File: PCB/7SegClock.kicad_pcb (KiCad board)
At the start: 2 copper layers, 177.8 x 76.2 mm, 41 parts, among them CON1 USB-MINI-B, Q1 NPN, U1 P8X32A, U2 24LC256, U3 FT232RL, U4 DS3231, U5 TPS62172DSGT, U6 LCMX02-640UHC-4TG144C, X1 5mhz CRYSTAL

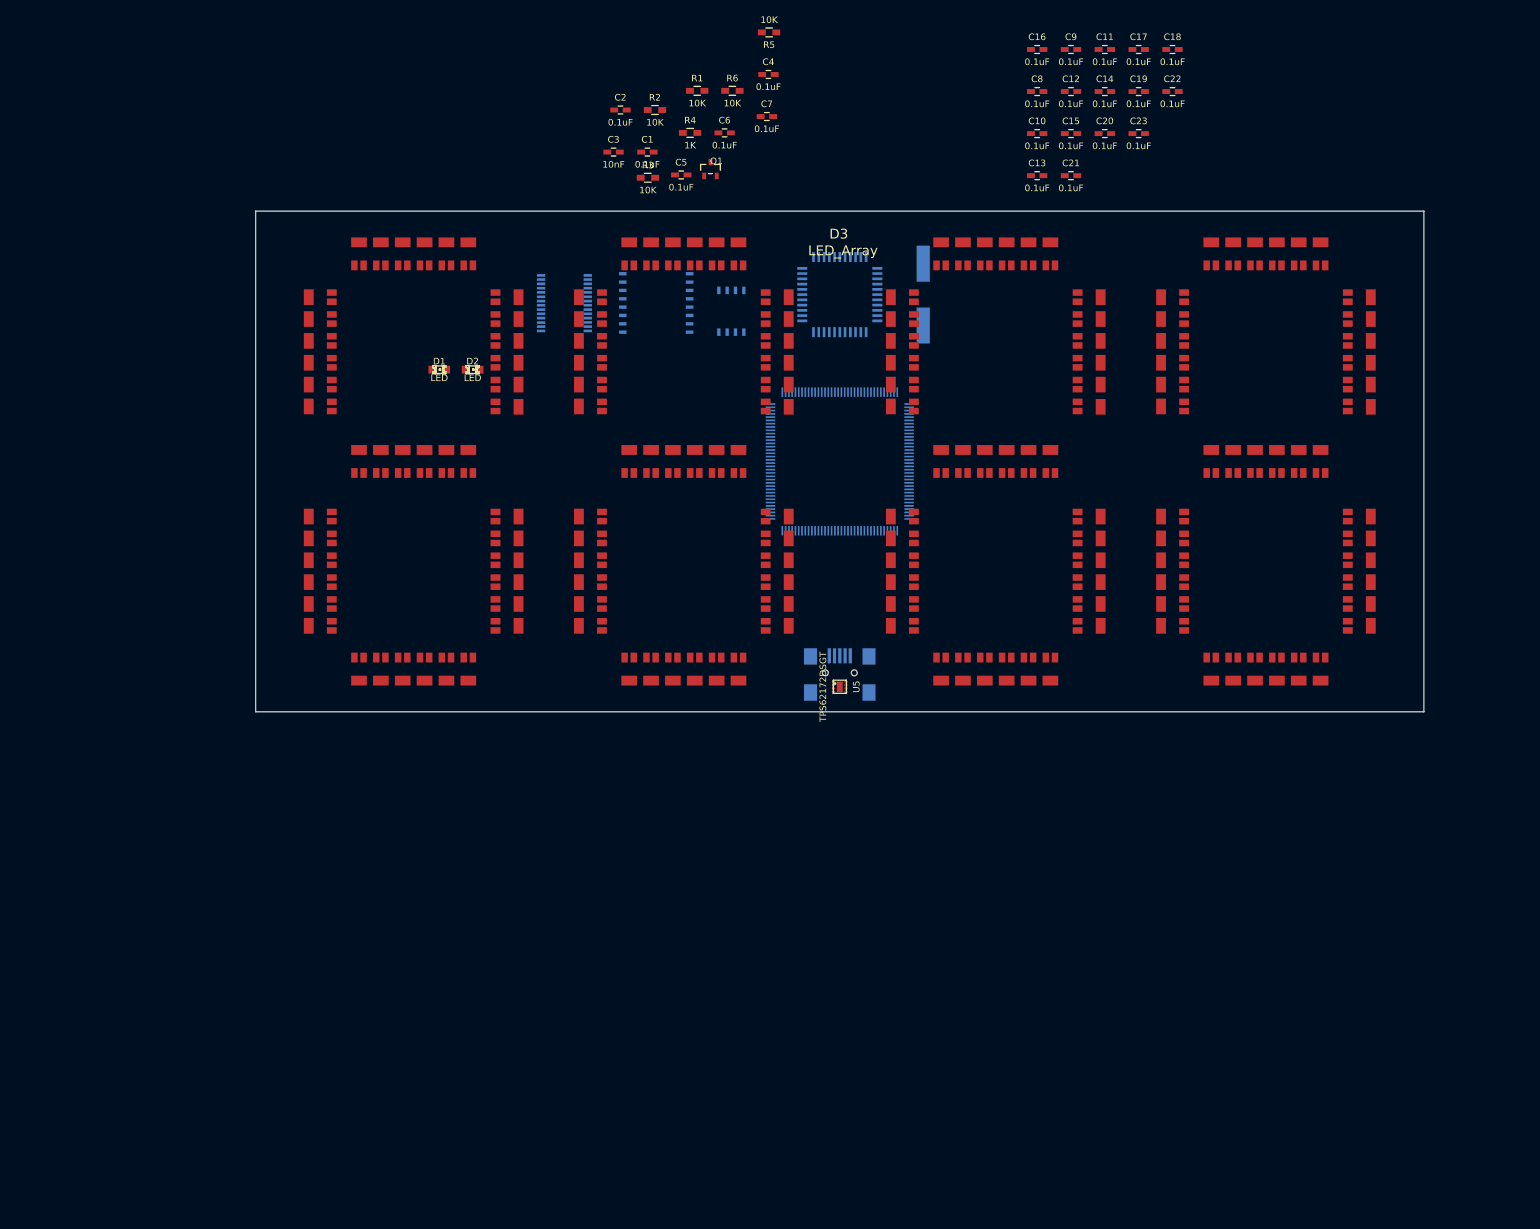
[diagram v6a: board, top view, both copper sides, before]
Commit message: Added additional mosfets.
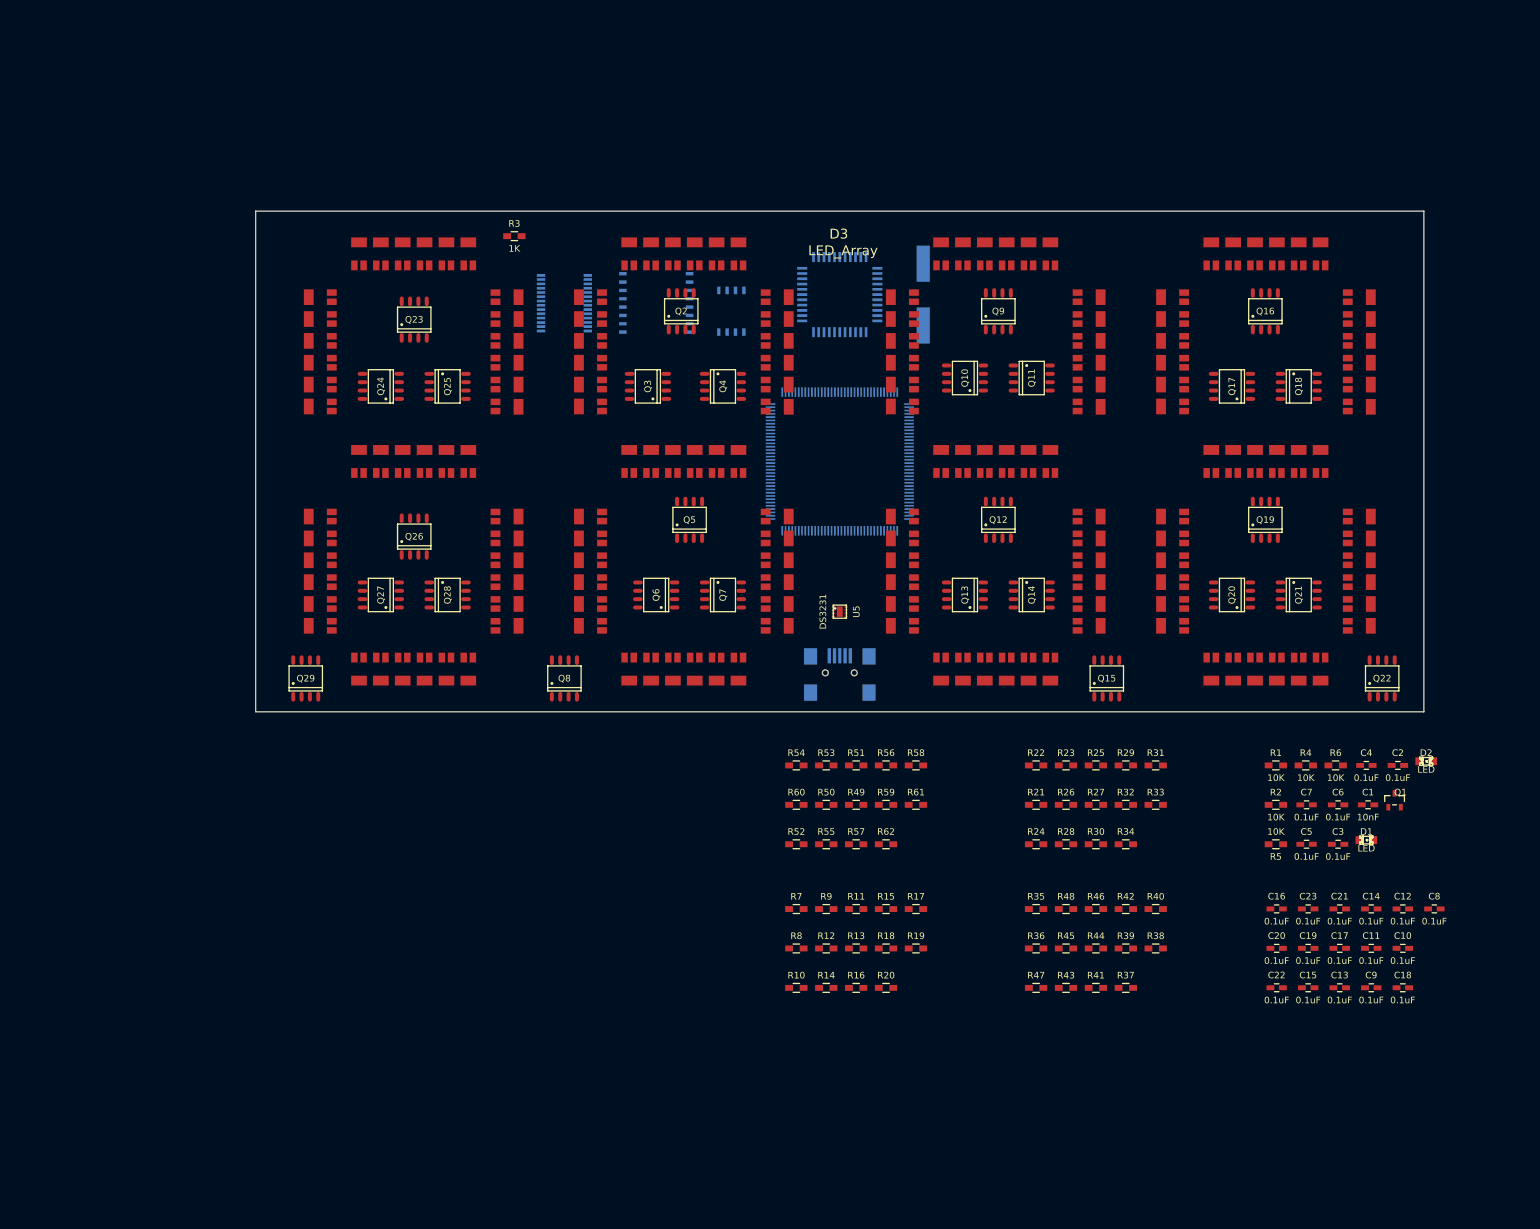
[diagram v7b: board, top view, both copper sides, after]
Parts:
- added Q10: DMN2041LSD-13, SO-8, F.Cu at (167.6, 73.7)
- added Q11: DMN2041LSD-13, SO-8, F.Cu at (177.8, 73.7)
- added Q12: DMN2041LSD-13, SO-8, F.Cu at (172.7, 95.2)
- added Q13: DMN2041LSD-13, SO-8, F.Cu at (167.6, 106.7)
- added Q14: DMN2041LSD-13, SO-8, F.Cu at (177.8, 106.7)
- added Q15: DMN2041LSD-13, SO-8, F.Cu at (189.2, 119.4)
- added Q16: DMN2041LSD-13, SO-8, F.Cu at (213.4, 63.5)
- added Q17: DMN2041LSD-13, SO-8, F.Cu at (208.3, 74.9)
- added Q18: DMN2041LSD-13, SO-8, F.Cu at (218.4, 74.9)
- added Q19: DMN2041LSD-13, SO-8, F.Cu at (213.4, 95.2)
- added Q2: DMN2041LSD-13, SO-8, F.Cu at (124.5, 63.5)
- added Q20: DMN2041LSD-13, SO-8, F.Cu at (208.3, 106.7)
- added Q21: DMN2041LSD-13, SO-8, F.Cu at (218.4, 106.7)
- added Q22: DMN2041LSD-13, SO-8, F.Cu at (231.1, 119.4)
- added Q23: DMN2041LSD-13, SO-8, F.Cu at (83.8, 64.8)
- added Q24: DMN2041LSD-13, SO-8, F.Cu at (78.7, 74.9)
- added Q25: DMN2041LSD-13, SO-8, F.Cu at (88.9, 74.9)
- added Q26: DMN2041LSD-13, SO-8, F.Cu at (83.8, 97.8)
- added Q27: DMN2041LSD-13, SO-8, F.Cu at (78.7, 106.7)
- added Q28: DMN2041LSD-13, SO-8, F.Cu at (88.9, 106.7)
- added Q29: DMN2041LSD-13, SO-8, F.Cu at (67.3, 119.4)
- added Q3: DMN2041LSD-13, SO-8, F.Cu at (119.4, 74.9)
- added Q4: DMN2041LSD-13, SO-8, F.Cu at (130.8, 74.9)
- added Q5: DMN2041LSD-13, SO-8, F.Cu at (125.7, 95.2)
- added Q6: DMN2041LSD-13, SO-8, F.Cu at (120.7, 106.7)
- added Q7: DMN2041LSD-13, SO-8, F.Cu at (130.8, 106.7)
- added Q8: DMN2041LSD-13, SO-8, F.Cu at (106.7, 119.4)
- added Q9: DMN2041LSD-13, SO-8, F.Cu at (172.7, 63.5)
- added R10: 10K, Resistors_SMD:R_0603_HandSoldering, F.Cu at (142.0, 166.5)
- added R11: 10K, Resistors_SMD:R_0603_HandSoldering, F.Cu at (151.1, 154.5)
- added R12: 10K, Resistors_SMD:R_0603_HandSoldering, F.Cu at (146.5, 160.5)
- added R13: 10K, Resistors_SMD:R_0603_HandSoldering, F.Cu at (151.1, 160.5)
- added R14: 10K, Resistors_SMD:R_0603_HandSoldering, F.Cu at (146.5, 166.5)
- added R15: 10K, Resistors_SMD:R_0603_HandSoldering, F.Cu at (155.6, 154.5)
- added R16: 10K, Resistors_SMD:R_0603_HandSoldering, F.Cu at (151.1, 166.5)
- added R17: 10K, Resistors_SMD:R_0603_HandSoldering, F.Cu at (160.2, 154.5)
- added R18: 10K, Resistors_SMD:R_0603_HandSoldering, F.Cu at (155.6, 160.5)
- added R19: 10K, Resistors_SMD:R_0603_HandSoldering, F.Cu at (160.2, 160.5)
- added R20: 10K, Resistors_SMD:R_0603_HandSoldering, F.Cu at (155.6, 166.5)
- added R21: 10K, Resistors_SMD:R_0603_HandSoldering, F.Cu at (178.5, 138.6)
- added R22: 10K, Resistors_SMD:R_0603_HandSoldering, F.Cu at (178.5, 132.6)
- added R23: 10K, Resistors_SMD:R_0603_HandSoldering, F.Cu at (183.0, 132.6)
- added R24: 10K, Resistors_SMD:R_0603_HandSoldering, F.Cu at (178.5, 144.6)
- added R25: 10K, Resistors_SMD:R_0603_HandSoldering, F.Cu at (187.6, 132.6)
- added R26: 10K, Resistors_SMD:R_0603_HandSoldering, F.Cu at (183.0, 138.6)
- added R27: 10K, Resistors_SMD:R_0603_HandSoldering, F.Cu at (187.6, 138.6)
- added R28: 10K, Resistors_SMD:R_0603_HandSoldering, F.Cu at (183.0, 144.6)
- added R29: 10K, Resistors_SMD:R_0603_HandSoldering, F.Cu at (192.1, 132.6)
- added R30: 10K, Resistors_SMD:R_0603_HandSoldering, F.Cu at (187.6, 144.6)
- added R31: 10K, Resistors_SMD:R_0603_HandSoldering, F.Cu at (196.7, 132.6)
- added R32: 10K, Resistors_SMD:R_0603_HandSoldering, F.Cu at (192.1, 138.6)
- added R33: 10K, Resistors_SMD:R_0603_HandSoldering, F.Cu at (196.7, 138.6)
- added R34: 10K, Resistors_SMD:R_0603_HandSoldering, F.Cu at (192.1, 144.6)
- added R35: 10K, Resistors_SMD:R_0603_HandSoldering, F.Cu at (178.5, 154.5)
- added R36: 10K, Resistors_SMD:R_0603_HandSoldering, F.Cu at (178.5, 160.5)
- added R37: 10K, Resistors_SMD:R_0603_HandSoldering, F.Cu at (192.1, 166.5)
- added R38: 10K, Resistors_SMD:R_0603_HandSoldering, F.Cu at (196.7, 160.5)
- added R39: 10K, Resistors_SMD:R_0603_HandSoldering, F.Cu at (192.1, 160.5)
- added R40: 10K, Resistors_SMD:R_0603_HandSoldering, F.Cu at (196.7, 154.5)
- added R41: 10K, Resistors_SMD:R_0603_HandSoldering, F.Cu at (187.6, 166.5)
- added R42: 10K, Resistors_SMD:R_0603_HandSoldering, F.Cu at (192.1, 154.5)
- added R43: 10K, Resistors_SMD:R_0603_HandSoldering, F.Cu at (183.0, 166.5)
- added R44: 10K, Resistors_SMD:R_0603_HandSoldering, F.Cu at (187.6, 160.5)
- added R45: 10K, Resistors_SMD:R_0603_HandSoldering, F.Cu at (183.0, 160.5)
- added R46: 10K, Resistors_SMD:R_0603_HandSoldering, F.Cu at (187.6, 154.5)
- added R47: 10K, Resistors_SMD:R_0603_HandSoldering, F.Cu at (178.5, 166.5)
- added R48: 10K, Resistors_SMD:R_0603_HandSoldering, F.Cu at (183.0, 154.5)
- added R49: 10K, Resistors_SMD:R_0603_HandSoldering, F.Cu at (151.1, 138.6)
- added R50: 10K, Resistors_SMD:R_0603_HandSoldering, F.Cu at (146.5, 138.6)
- added R51: 10K, Resistors_SMD:R_0603_HandSoldering, F.Cu at (151.1, 132.6)
- added R52: 10K, Resistors_SMD:R_0603_HandSoldering, F.Cu at (142.0, 144.6)
- added R53: 10K, Resistors_SMD:R_0603_HandSoldering, F.Cu at (146.5, 132.6)
- added R54: 10K, Resistors_SMD:R_0603_HandSoldering, F.Cu at (142.0, 132.6)
- added R55: 10K, Resistors_SMD:R_0603_HandSoldering, F.Cu at (146.5, 144.6)
- added R56: 10K, Resistors_SMD:R_0603_HandSoldering, F.Cu at (155.6, 132.6)
- added R57: 10K, Resistors_SMD:R_0603_HandSoldering, F.Cu at (151.1, 144.6)
- added R58: 10K, Resistors_SMD:R_0603_HandSoldering, F.Cu at (160.2, 132.6)
- added R59: 10K, Resistors_SMD:R_0603_HandSoldering, F.Cu at (155.6, 138.6)
- added R60: 10K, Resistors_SMD:R_0603_HandSoldering, F.Cu at (142.0, 138.6)
- added R61: 10K, Resistors_SMD:R_0603_HandSoldering, F.Cu at (160.2, 138.6)
- added R62: 10K, Resistors_SMD:R_0603_HandSoldering, F.Cu at (155.6, 144.6)
- added R7: 10K, Resistors_SMD:R_0603_HandSoldering, F.Cu at (142.0, 154.5)
- added R8: 10K, Resistors_SMD:R_0603_HandSoldering, F.Cu at (142.0, 160.5)
- added R9: 10K, Resistors_SMD:R_0603_HandSoldering, F.Cu at (146.5, 154.5)
- C1: value 0.1uF -> 10nF
- C3: value 10nF -> 0.1uF
- R3: value 10K -> 1K
- R4: value 1K -> 10K
- U1: value P8X32A -> TPS62172DSGT
- U2: value 24LC256 -> P8X32A
- U4: value DS3231 -> 24LC256
- U5: value TPS62172DSGT -> DS3231
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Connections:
- C1 pad 1: GND -> Net-(C1-Pad1)
- C1 pad 2: +3V3 -> Net-(C1-Pad2)
- C3 pad 1: Net-(C3-Pad1) -> GND
- C3 pad 2: Net-(C3-Pad2) -> +3V3
- D3 pad 1: Net-(D3-Pad1) -> /Lattice MACHXO2/Digit_1/D1A1
- D3 pad 10: Net-(D3-Pad10) -> /Lattice MACHXO2/Digit_1/D1A4
- D3 pad 100: Net-(D3-Pad100) -> /Lattice MACHXO2/Digit_1/D1A4
- D3 pad 103: Net-(D3-Pad103) -> /Lattice MACHXO2/Digit_1/D1A5
- D3 pad 104: Net-(D3-Pad104) -> Net-(D3-Pad101)
- D3 pad 105: Net-(D3-Pad105) -> Net-(D3-Pad102)
- D3 pad 106: Net-(D3-Pad106) -> /Lattice MACHXO2/Digit_1/D1A6
- D3 pad 107: Net-(D3-Pad107) -> Net-(D3-Pad101)
- D3 pad 108: Net-(D3-Pad108) -> Net-(D3-Pad102)
- D3 pad 109: Net-(D3-Pad109) -> /Lattice MACHXO2/Digit_1/D1A1
- D3 pad 112: Net-(D3-Pad112) -> /Lattice MACHXO2/Digit_1/D1A2
- D3 pad 113: Net-(D3-Pad113) -> Net-(D3-Pad110)
- D3 pad 114: Net-(D3-Pad114) -> Net-(D3-Pad111)
- D3 pad 115: Net-(D3-Pad115) -> /Lattice MACHXO2/Digit_1/D1A3
- D3 pad 116: Net-(D3-Pad116) -> Net-(D3-Pad110)
- D3 pad 117: Net-(D3-Pad117) -> Net-(D3-Pad111)
- D3 pad 118: Net-(D3-Pad118) -> /Lattice MACHXO2/Digit_1/D1A4
- D3 pad 119: Net-(D3-Pad119) -> Net-(D3-Pad110)
- D3 pad 120: Net-(D3-Pad120) -> Net-(D3-Pad111)
- D3 pad 121: Net-(D3-Pad121) -> /Lattice MACHXO2/Digit_1/D1A5
- D3 pad 122: Net-(D3-Pad122) -> Net-(D3-Pad110)
- D3 pad 123: Net-(D3-Pad123) -> Net-(D3-Pad111)
- D3 pad 124: Net-(D3-Pad124) -> /Lattice MACHXO2/Digit_1/D1A6
- D3 pad 125: Net-(D3-Pad125) -> Net-(D3-Pad110)
- D3 pad 126: Net-(D3-Pad126) -> Net-(D3-Pad111)
- D3 pad 127: Net-(D3-Pad127) -> /Lattice MACHXO2/Digit_2/D2A1
- D3 pad 13: Net-(D3-Pad13) -> /Lattice MACHXO2/Digit_1/D1A5
- D3 pad 130: Net-(D3-Pad130) -> /Lattice MACHXO2/Digit_2/D2A2
- D3 pad 131: Net-(D3-Pad131) -> Net-(D3-Pad128)
- D3 pad 132: Net-(D3-Pad132) -> Net-(D3-Pad129)
- D3 pad 133: Net-(D3-Pad133) -> /Lattice MACHXO2/Digit_2/D2A3
- D3 pad 134: Net-(D3-Pad134) -> Net-(D3-Pad128)
- D3 pad 135: Net-(D3-Pad135) -> Net-(D3-Pad129)
- D3 pad 136: Net-(D3-Pad136) -> /Lattice MACHXO2/Digit_2/D2A4
- D3 pad 137: Net-(D3-Pad137) -> Net-(D3-Pad128)
- D3 pad 138: Net-(D3-Pad138) -> Net-(D3-Pad129)
- D3 pad 139: Net-(D3-Pad139) -> /Lattice MACHXO2/Digit_2/D2A5
- D3 pad 14: Net-(D3-Pad14) -> Net-(D3-Pad11)
- D3 pad 140: Net-(D3-Pad140) -> Net-(D3-Pad128)
- D3 pad 141: Net-(D3-Pad141) -> Net-(D3-Pad129)
- D3 pad 142: Net-(D3-Pad142) -> /Lattice MACHXO2/Digit_2/D2A6
- D3 pad 143: Net-(D3-Pad143) -> Net-(D3-Pad128)
- D3 pad 144: Net-(D3-Pad144) -> Net-(D3-Pad129)
- D3 pad 145: Net-(D3-Pad145) -> /Lattice MACHXO2/Digit_2/D2A1
- D3 pad 148: Net-(D3-Pad148) -> /Lattice MACHXO2/Digit_2/D2A2
- D3 pad 149: Net-(D3-Pad149) -> Net-(D3-Pad146)
- D3 pad 15: Net-(D3-Pad15) -> Net-(D3-Pad12)
- D3 pad 150: Net-(D3-Pad150) -> Net-(D3-Pad147)
- D3 pad 151: Net-(D3-Pad151) -> /Lattice MACHXO2/Digit_2/D2A3
- D3 pad 152: Net-(D3-Pad152) -> Net-(D3-Pad146)
- D3 pad 153: Net-(D3-Pad153) -> Net-(D3-Pad147)
- D3 pad 154: Net-(D3-Pad154) -> /Lattice MACHXO2/Digit_2/D2A4
- D3 pad 155: Net-(D3-Pad155) -> Net-(D3-Pad146)
- D3 pad 156: Net-(D3-Pad156) -> Net-(D3-Pad147)
- D3 pad 157: Net-(D3-Pad157) -> /Lattice MACHXO2/Digit_2/D2A5
- D3 pad 158: Net-(D3-Pad158) -> Net-(D3-Pad146)
- D3 pad 159: Net-(D3-Pad159) -> Net-(D3-Pad147)
- D3 pad 16: Net-(D3-Pad16) -> /Lattice MACHXO2/Digit_1/D1A6
- D3 pad 160: Net-(D3-Pad160) -> /Lattice MACHXO2/Digit_2/D2A6
- D3 pad 161: Net-(D3-Pad161) -> Net-(D3-Pad146)
- D3 pad 162: Net-(D3-Pad162) -> Net-(D3-Pad147)
- D3 pad 163: Net-(D3-Pad163) -> /Lattice MACHXO2/Digit_2/D2A1
- D3 pad 166: Net-(D3-Pad166) -> /Lattice MACHXO2/Digit_2/D2A2
- D3 pad 167: Net-(D3-Pad167) -> Net-(D3-Pad164)
- D3 pad 168: Net-(D3-Pad168) -> Net-(D3-Pad165)
- D3 pad 169: Net-(D3-Pad169) -> /Lattice MACHXO2/Digit_2/D2A3
- D3 pad 17: Net-(D3-Pad17) -> Net-(D3-Pad11)
- D3 pad 170: Net-(D3-Pad170) -> Net-(D3-Pad164)
- D3 pad 171: Net-(D3-Pad171) -> Net-(D3-Pad165)
- D3 pad 172: Net-(D3-Pad172) -> /Lattice MACHXO2/Digit_2/D2A4
- D3 pad 173: Net-(D3-Pad173) -> Net-(D3-Pad164)
- D3 pad 174: Net-(D3-Pad174) -> Net-(D3-Pad165)
- D3 pad 175: Net-(D3-Pad175) -> /Lattice MACHXO2/Digit_2/D2A5
- D3 pad 176: Net-(D3-Pad176) -> Net-(D3-Pad164)
- D3 pad 177: Net-(D3-Pad177) -> Net-(D3-Pad165)
- D3 pad 178: Net-(D3-Pad178) -> /Lattice MACHXO2/Digit_2/D2A6
- D3 pad 179: Net-(D3-Pad179) -> Net-(D3-Pad164)
- D3 pad 18: Net-(D3-Pad18) -> Net-(D3-Pad12)
- D3 pad 180: Net-(D3-Pad180) -> Net-(D3-Pad165)
- D3 pad 181: Net-(D3-Pad181) -> /Lattice MACHXO2/Digit_2/D2A1
- D3 pad 184: Net-(D3-Pad184) -> /Lattice MACHXO2/Digit_2/D2A2
- D3 pad 185: Net-(D3-Pad185) -> Net-(D3-Pad182)
- D3 pad 186: Net-(D3-Pad186) -> Net-(D3-Pad183)
- D3 pad 187: Net-(D3-Pad187) -> /Lattice MACHXO2/Digit_2/D2A3
- D3 pad 188: Net-(D3-Pad188) -> Net-(D3-Pad182)
- D3 pad 189: Net-(D3-Pad189) -> Net-(D3-Pad183)
- D3 pad 19: Net-(D3-Pad19) -> /Lattice MACHXO2/Digit_1/D1A1
- D3 pad 190: Net-(D3-Pad190) -> /Lattice MACHXO2/Digit_2/D2A4
- D3 pad 191: Net-(D3-Pad191) -> Net-(D3-Pad182)
- D3 pad 192: Net-(D3-Pad192) -> Net-(D3-Pad183)
- D3 pad 193: Net-(D3-Pad193) -> /Lattice MACHXO2/Digit_2/D2A5
- D3 pad 194: Net-(D3-Pad194) -> Net-(D3-Pad182)
- D3 pad 195: Net-(D3-Pad195) -> Net-(D3-Pad183)
- D3 pad 196: Net-(D3-Pad196) -> /Lattice MACHXO2/Digit_2/D2A6
- D3 pad 197: Net-(D3-Pad197) -> Net-(D3-Pad182)
- D3 pad 198: Net-(D3-Pad198) -> Net-(D3-Pad183)
- D3 pad 199: Net-(D3-Pad199) -> /Lattice MACHXO2/Digit_2/D2A1
- D3 pad 2: Net-(D3-Pad2) -> Net-(D3-Pad11)
- D3 pad 202: Net-(D3-Pad202) -> /Lattice MACHXO2/Digit_2/D2A2
- D3 pad 203: Net-(D3-Pad203) -> Net-(D3-Pad200)
- D3 pad 204: Net-(D3-Pad204) -> Net-(D3-Pad201)
- D3 pad 205: Net-(D3-Pad205) -> /Lattice MACHXO2/Digit_2/D2A3
- D3 pad 206: Net-(D3-Pad206) -> Net-(D3-Pad200)
- D3 pad 207: Net-(D3-Pad207) -> Net-(D3-Pad201)
- D3 pad 208: Net-(D3-Pad208) -> /Lattice MACHXO2/Digit_2/D2A4
- D3 pad 209: Net-(D3-Pad209) -> Net-(D3-Pad200)
- D3 pad 210: Net-(D3-Pad210) -> Net-(D3-Pad201)
- D3 pad 211: Net-(D3-Pad211) -> /Lattice MACHXO2/Digit_2/D2A5
- D3 pad 212: Net-(D3-Pad212) -> Net-(D3-Pad200)
- D3 pad 213: Net-(D3-Pad213) -> Net-(D3-Pad201)
- D3 pad 214: Net-(D3-Pad214) -> /Lattice MACHXO2/Digit_2/D2A6
- D3 pad 215: Net-(D3-Pad215) -> Net-(D3-Pad200)
- D3 pad 216: Net-(D3-Pad216) -> Net-(D3-Pad201)
- D3 pad 217: Net-(D3-Pad217) -> /Lattice MACHXO2/Digit_2/D2A1
- D3 pad 22: Net-(D3-Pad22) -> /Lattice MACHXO2/Digit_1/D1A2
- D3 pad 220: Net-(D3-Pad220) -> /Lattice MACHXO2/Digit_2/D2A2
- D3 pad 221: Net-(D3-Pad221) -> Net-(D3-Pad218)
- D3 pad 222: Net-(D3-Pad222) -> Net-(D3-Pad219)
- D3 pad 223: Net-(D3-Pad223) -> /Lattice MACHXO2/Digit_2/D2A3
- D3 pad 224: Net-(D3-Pad224) -> Net-(D3-Pad218)
- D3 pad 225: Net-(D3-Pad225) -> Net-(D3-Pad219)
- D3 pad 226: Net-(D3-Pad226) -> /Lattice MACHXO2/Digit_2/D2A4
- D3 pad 227: Net-(D3-Pad227) -> Net-(D3-Pad218)
- D3 pad 228: Net-(D3-Pad228) -> Net-(D3-Pad219)
- D3 pad 229: Net-(D3-Pad229) -> /Lattice MACHXO2/Digit_2/D2A5
- D3 pad 23: Net-(D3-Pad23) -> Net-(D3-Pad20)
- D3 pad 230: Net-(D3-Pad230) -> Net-(D3-Pad218)
- D3 pad 231: Net-(D3-Pad231) -> Net-(D3-Pad219)
- D3 pad 232: Net-(D3-Pad232) -> /Lattice MACHXO2/Digit_2/D2A6
- D3 pad 233: Net-(D3-Pad233) -> Net-(D3-Pad218)
- D3 pad 234: Net-(D3-Pad234) -> Net-(D3-Pad219)
- D3 pad 235: Net-(D3-Pad235) -> /Lattice MACHXO2/Digit_2/D2A1
- D3 pad 238: Net-(D3-Pad238) -> /Lattice MACHXO2/Digit_2/D2A2
- D3 pad 239: Net-(D3-Pad239) -> Net-(D3-Pad236)
- D3 pad 24: Net-(D3-Pad24) -> Net-(D3-Pad21)
- D3 pad 240: Net-(D3-Pad240) -> Net-(D3-Pad237)
- D3 pad 241: Net-(D3-Pad241) -> /Lattice MACHXO2/Digit_2/D2A3
- D3 pad 243: Net-(D3-Pad243) -> Net-(D3-Pad237)
- D3 pad 244: Net-(D3-Pad244) -> /Lattice MACHXO2/Digit_2/D2A4
- D3 pad 245: Net-(D3-Pad245) -> Net-(D3-Pad236)
- D3 pad 246: Net-(D3-Pad246) -> Net-(D3-Pad237)
- D3 pad 247: Net-(D3-Pad247) -> /Lattice MACHXO2/Digit_2/D2A5
- D3 pad 248: Net-(D3-Pad248) -> Net-(D3-Pad236)
- D3 pad 249: Net-(D3-Pad249) -> Net-(D3-Pad237)
- D3 pad 25: Net-(D3-Pad25) -> /Lattice MACHXO2/Digit_1/D1A3
- D3 pad 250: Net-(D3-Pad250) -> /Lattice MACHXO2/Digit_2/D2A6
- D3 pad 251: Net-(D3-Pad251) -> Net-(D3-Pad236)
- D3 pad 252: Net-(D3-Pad252) -> Net-(D3-Pad237)
- D3 pad 253: Net-(D3-Pad253) -> /Lattice MACHXO2/Digit_3/D3A1
- D3 pad 256: Net-(D3-Pad256) -> /Lattice MACHXO2/Digit_3/D3A2
- D3 pad 257: Net-(D3-Pad257) -> Net-(D3-Pad254)
- D3 pad 258: Net-(D3-Pad258) -> Net-(D3-Pad255)
- D3 pad 259: Net-(D3-Pad259) -> /Lattice MACHXO2/Digit_3/D3A3
- D3 pad 26: Net-(D3-Pad26) -> Net-(D3-Pad20)
- D3 pad 260: Net-(D3-Pad260) -> Net-(D3-Pad254)
- D3 pad 261: Net-(D3-Pad261) -> Net-(D3-Pad255)
- D3 pad 262: Net-(D3-Pad262) -> /Lattice MACHXO2/Digit_3/D3A4
- D3 pad 263: Net-(D3-Pad263) -> Net-(D3-Pad254)
- D3 pad 264: Net-(D3-Pad264) -> Net-(D3-Pad255)
- D3 pad 265: Net-(D3-Pad265) -> /Lattice MACHXO2/Digit_3/D3A5
- D3 pad 266: Net-(D3-Pad266) -> Net-(D3-Pad254)
- D3 pad 267: Net-(D3-Pad267) -> Net-(D3-Pad255)
- D3 pad 268: Net-(D3-Pad268) -> /Lattice MACHXO2/Digit_3/D3A6
- D3 pad 269: Net-(D3-Pad269) -> Net-(D3-Pad254)
- D3 pad 27: Net-(D3-Pad27) -> Net-(D3-Pad21)
- D3 pad 270: Net-(D3-Pad270) -> Net-(D3-Pad255)
- D3 pad 271: Net-(D3-Pad271) -> /Lattice MACHXO2/Digit_3/D3A1
- D3 pad 274: Net-(D3-Pad274) -> /Lattice MACHXO2/Digit_3/D3A2
- D3 pad 275: Net-(D3-Pad275) -> Net-(D3-Pad272)
- D3 pad 276: Net-(D3-Pad276) -> Net-(D3-Pad273)
- D3 pad 277: Net-(D3-Pad277) -> /Lattice MACHXO2/Digit_3/D3A3
- D3 pad 278: Net-(D3-Pad278) -> Net-(D3-Pad272)
- D3 pad 279: Net-(D3-Pad279) -> Net-(D3-Pad273)
- D3 pad 28: Net-(D3-Pad28) -> /Lattice MACHXO2/Digit_1/D1A4
- D3 pad 280: Net-(D3-Pad280) -> /Lattice MACHXO2/Digit_3/D3A4
- D3 pad 281: Net-(D3-Pad281) -> Net-(D3-Pad272)
- D3 pad 282: Net-(D3-Pad282) -> Net-(D3-Pad273)
- D3 pad 283: Net-(D3-Pad283) -> /Lattice MACHXO2/Digit_3/D3A5
- D3 pad 284: Net-(D3-Pad284) -> Net-(D3-Pad272)
- D3 pad 285: Net-(D3-Pad285) -> Net-(D3-Pad273)
- D3 pad 286: Net-(D3-Pad286) -> /Lattice MACHXO2/Digit_3/D3A6
- D3 pad 287: Net-(D3-Pad287) -> Net-(D3-Pad272)
- D3 pad 288: Net-(D3-Pad288) -> Net-(D3-Pad273)
- D3 pad 289: Net-(D3-Pad289) -> /Lattice MACHXO2/Digit_3/D3A1
- D3 pad 29: Net-(D3-Pad29) -> Net-(D3-Pad20)
- D3 pad 292: Net-(D3-Pad292) -> /Lattice MACHXO2/Digit_3/D3A2
- D3 pad 293: Net-(D3-Pad293) -> Net-(D3-Pad290)
- D3 pad 294: Net-(D3-Pad294) -> Net-(D3-Pad291)
- D3 pad 295: Net-(D3-Pad295) -> /Lattice MACHXO2/Digit_3/D3A3
- D3 pad 296: Net-(D3-Pad296) -> Net-(D3-Pad290)
- D3 pad 297: Net-(D3-Pad297) -> Net-(D3-Pad291)
- D3 pad 298: Net-(D3-Pad298) -> /Lattice MACHXO2/Digit_3/D3A4
- D3 pad 299: Net-(D3-Pad299) -> Net-(D3-Pad290)
- D3 pad 3: Net-(D3-Pad3) -> Net-(D3-Pad12)
- D3 pad 30: Net-(D3-Pad30) -> Net-(D3-Pad21)
- D3 pad 300: Net-(D3-Pad300) -> Net-(D3-Pad291)
- D3 pad 301: Net-(D3-Pad301) -> /Lattice MACHXO2/Digit_3/D3A5
- D3 pad 302: Net-(D3-Pad302) -> Net-(D3-Pad290)
- D3 pad 303: Net-(D3-Pad303) -> Net-(D3-Pad291)
- D3 pad 304: Net-(D3-Pad304) -> /Lattice MACHXO2/Digit_3/D3A6
- D3 pad 305: Net-(D3-Pad305) -> Net-(D3-Pad290)
- D3 pad 306: Net-(D3-Pad306) -> Net-(D3-Pad291)
- D3 pad 307: Net-(D3-Pad307) -> /Lattice MACHXO2/Digit_3/D3A1
- D3 pad 31: Net-(D3-Pad31) -> /Lattice MACHXO2/Digit_1/D1A5
- D3 pad 310: Net-(D3-Pad310) -> /Lattice MACHXO2/Digit_3/D3A2
- D3 pad 311: Net-(D3-Pad311) -> Net-(D3-Pad308)
- D3 pad 312: Net-(D3-Pad312) -> Net-(D3-Pad309)
- D3 pad 313: Net-(D3-Pad313) -> /Lattice MACHXO2/Digit_3/D3A3
- D3 pad 314: Net-(D3-Pad314) -> Net-(D3-Pad308)
- D3 pad 315: Net-(D3-Pad315) -> Net-(D3-Pad309)
- D3 pad 316: Net-(D3-Pad316) -> /Lattice MACHXO2/Digit_3/D3A4
- D3 pad 317: Net-(D3-Pad317) -> Net-(D3-Pad308)
- D3 pad 318: Net-(D3-Pad318) -> Net-(D3-Pad309)
- D3 pad 319: Net-(D3-Pad319) -> /Lattice MACHXO2/Digit_3/D3A5
- D3 pad 32: Net-(D3-Pad32) -> Net-(D3-Pad20)
- D3 pad 320: Net-(D3-Pad320) -> Net-(D3-Pad308)
- D3 pad 321: Net-(D3-Pad321) -> Net-(D3-Pad309)
- D3 pad 322: Net-(D3-Pad322) -> /Lattice MACHXO2/Digit_3/D3A6
- D3 pad 323: Net-(D3-Pad323) -> Net-(D3-Pad308)
- D3 pad 324: Net-(D3-Pad324) -> Net-(D3-Pad309)
- D3 pad 325: Net-(D3-Pad325) -> /Lattice MACHXO2/Digit_3/D3A1
- D3 pad 328: Net-(D3-Pad328) -> /Lattice MACHXO2/Digit_3/D3A2
- D3 pad 329: Net-(D3-Pad329) -> Net-(D3-Pad326)
- D3 pad 33: Net-(D3-Pad33) -> Net-(D3-Pad21)
- D3 pad 330: Net-(D3-Pad330) -> Net-(D3-Pad327)
- D3 pad 331: Net-(D3-Pad331) -> /Lattice MACHXO2/Digit_3/D3A3
- D3 pad 332: Net-(D3-Pad332) -> Net-(D3-Pad326)
- D3 pad 333: Net-(D3-Pad333) -> Net-(D3-Pad327)
- D3 pad 334: Net-(D3-Pad334) -> /Lattice MACHXO2/Digit_3/D3A4
- D3 pad 335: Net-(D3-Pad335) -> Net-(D3-Pad326)
- D3 pad 336: Net-(D3-Pad336) -> Net-(D3-Pad327)
- D3 pad 337: Net-(D3-Pad337) -> /Lattice MACHXO2/Digit_3/D3A5
- D3 pad 338: Net-(D3-Pad338) -> Net-(D3-Pad326)
- D3 pad 339: Net-(D3-Pad339) -> Net-(D3-Pad327)
- D3 pad 34: Net-(D3-Pad34) -> /Lattice MACHXO2/Digit_1/D1A6
- D3 pad 340: Net-(D3-Pad340) -> /Lattice MACHXO2/Digit_3/D3A6
- D3 pad 341: Net-(D3-Pad341) -> Net-(D3-Pad326)
- D3 pad 342: Net-(D3-Pad342) -> Net-(D3-Pad327)
- D3 pad 343: Net-(D3-Pad343) -> /Lattice MACHXO2/Digit_3/D3A1
- D3 pad 346: Net-(D3-Pad346) -> /Lattice MACHXO2/Digit_3/D3A2
- D3 pad 347: Net-(D3-Pad347) -> Net-(D3-Pad344)
- D3 pad 348: Net-(D3-Pad348) -> Net-(D3-Pad345)
- D3 pad 349: Net-(D3-Pad349) -> /Lattice MACHXO2/Digit_3/D3A3
- D3 pad 35: Net-(D3-Pad35) -> Net-(D3-Pad20)
- D3 pad 350: Net-(D3-Pad350) -> Net-(D3-Pad344)
- D3 pad 351: Net-(D3-Pad351) -> Net-(D3-Pad345)
- D3 pad 352: Net-(D3-Pad352) -> /Lattice MACHXO2/Digit_3/D3A4
- D3 pad 353: Net-(D3-Pad353) -> Net-(D3-Pad344)
- D3 pad 354: Net-(D3-Pad354) -> Net-(D3-Pad345)
- D3 pad 355: Net-(D3-Pad355) -> /Lattice MACHXO2/Digit_3/D3A5
- D3 pad 356: Net-(D3-Pad356) -> Net-(D3-Pad344)
- D3 pad 357: Net-(D3-Pad357) -> Net-(D3-Pad345)
- D3 pad 358: Net-(D3-Pad358) -> /Lattice MACHXO2/Digit_3/D3A6
- D3 pad 359: Net-(D3-Pad359) -> Net-(D3-Pad344)
- D3 pad 36: Net-(D3-Pad36) -> Net-(D3-Pad21)
- D3 pad 360: Net-(D3-Pad360) -> Net-(D3-Pad345)
- D3 pad 361: Net-(D3-Pad361) -> /Lattice MACHXO2/Digit_3/D3A1
- D3 pad 364: Net-(D3-Pad364) -> /Lattice MACHXO2/Digit_3/D3A2
- D3 pad 365: Net-(D3-Pad365) -> Net-(D3-Pad362)
- D3 pad 366: Net-(D3-Pad366) -> Net-(D3-Pad363)
- D3 pad 367: Net-(D3-Pad367) -> /Lattice MACHXO2/Digit_3/D3A3
- D3 pad 369: Net-(D3-Pad369) -> Net-(D3-Pad363)
- D3 pad 37: Net-(D3-Pad37) -> /Lattice MACHXO2/Digit_1/D1A1
- D3 pad 370: Net-(D3-Pad370) -> /Lattice MACHXO2/Digit_3/D3A4
- D3 pad 371: Net-(D3-Pad371) -> Net-(D3-Pad362)
- D3 pad 372: Net-(D3-Pad372) -> Net-(D3-Pad363)
- D3 pad 373: Net-(D3-Pad373) -> /Lattice MACHXO2/Digit_3/D3A5
- D3 pad 374: Net-(D3-Pad374) -> Net-(D3-Pad362)
- D3 pad 375: Net-(D3-Pad375) -> Net-(D3-Pad363)
- D3 pad 376: Net-(D3-Pad376) -> /Lattice MACHXO2/Digit_3/D3A6
- D3 pad 377: Net-(D3-Pad377) -> Net-(D3-Pad362)
- D3 pad 378: Net-(D3-Pad378) -> Net-(D3-Pad363)
- D3 pad 379: Net-(D3-Pad379) -> /Lattice MACHXO2/Digit_4/D4A1
- D3 pad 382: Net-(D3-Pad382) -> /Lattice MACHXO2/Digit_4/D4A2
- D3 pad 383: Net-(D3-Pad383) -> Net-(D3-Pad380)
- D3 pad 384: Net-(D3-Pad384) -> Net-(D3-Pad381)
- D3 pad 385: Net-(D3-Pad385) -> /Lattice MACHXO2/Digit_4/D4A3
- D3 pad 386: Net-(D3-Pad386) -> Net-(D3-Pad380)
- D3 pad 387: Net-(D3-Pad387) -> Net-(D3-Pad381)
- D3 pad 388: Net-(D3-Pad388) -> /Lattice MACHXO2/Digit_4/D4A4
- D3 pad 389: Net-(D3-Pad389) -> Net-(D3-Pad380)
- D3 pad 390: Net-(D3-Pad390) -> Net-(D3-Pad381)
- D3 pad 391: Net-(D3-Pad391) -> /Lattice MACHXO2/Digit_4/D4A5
- D3 pad 392: Net-(D3-Pad392) -> Net-(D3-Pad380)
- D3 pad 393: Net-(D3-Pad393) -> Net-(D3-Pad381)
- D3 pad 394: Net-(D3-Pad394) -> /Lattice MACHXO2/Digit_4/D4A6
- D3 pad 395: Net-(D3-Pad395) -> Net-(D3-Pad380)
- D3 pad 396: Net-(D3-Pad396) -> Net-(D3-Pad381)
- D3 pad 397: Net-(D3-Pad397) -> /Lattice MACHXO2/Digit_4/D4A1
- D3 pad 4: Net-(D3-Pad4) -> /Lattice MACHXO2/Digit_1/D1A2
- D3 pad 40: Net-(D3-Pad40) -> /Lattice MACHXO2/Digit_1/D1A2
- D3 pad 400: Net-(D3-Pad400) -> /Lattice MACHXO2/Digit_4/D4A2
- D3 pad 401: Net-(D3-Pad401) -> Net-(D3-Pad398)
- D3 pad 402: Net-(D3-Pad402) -> Net-(D3-Pad399)
- D3 pad 403: Net-(D3-Pad403) -> /Lattice MACHXO2/Digit_4/D4A3
- D3 pad 404: Net-(D3-Pad404) -> Net-(D3-Pad398)
- D3 pad 405: Net-(D3-Pad405) -> Net-(D3-Pad399)
- D3 pad 406: Net-(D3-Pad406) -> /Lattice MACHXO2/Digit_4/D4A4
- D3 pad 407: Net-(D3-Pad407) -> Net-(D3-Pad398)
- D3 pad 408: Net-(D3-Pad408) -> Net-(D3-Pad399)
- D3 pad 409: Net-(D3-Pad409) -> /Lattice MACHXO2/Digit_4/D4A5
- D3 pad 41: Net-(D3-Pad41) -> Net-(D3-Pad38)
- D3 pad 410: Net-(D3-Pad410) -> Net-(D3-Pad398)
- D3 pad 411: Net-(D3-Pad411) -> Net-(D3-Pad399)
- D3 pad 412: Net-(D3-Pad412) -> /Lattice MACHXO2/Digit_4/D4A6
- D3 pad 413: Net-(D3-Pad413) -> Net-(D3-Pad398)
- D3 pad 414: Net-(D3-Pad414) -> Net-(D3-Pad399)
- D3 pad 415: Net-(D3-Pad415) -> /Lattice MACHXO2/Digit_4/D4A1
- D3 pad 418: Net-(D3-Pad418) -> /Lattice MACHXO2/Digit_4/D4A2
- D3 pad 419: Net-(D3-Pad419) -> Net-(D3-Pad416)
- D3 pad 42: Net-(D3-Pad42) -> Net-(D3-Pad39)
- D3 pad 420: Net-(D3-Pad420) -> Net-(D3-Pad417)
- D3 pad 421: Net-(D3-Pad421) -> /Lattice MACHXO2/Digit_4/D4A3
- D3 pad 422: Net-(D3-Pad422) -> Net-(D3-Pad416)
- D3 pad 423: Net-(D3-Pad423) -> Net-(D3-Pad417)
- D3 pad 424: Net-(D3-Pad424) -> /Lattice MACHXO2/Digit_4/D4A4
- D3 pad 425: Net-(D3-Pad425) -> Net-(D3-Pad416)
- D3 pad 426: Net-(D3-Pad426) -> Net-(D3-Pad417)
- D3 pad 427: Net-(D3-Pad427) -> /Lattice MACHXO2/Digit_4/D4A5
- D3 pad 428: Net-(D3-Pad428) -> Net-(D3-Pad416)
- D3 pad 429: Net-(D3-Pad429) -> Net-(D3-Pad417)
- D3 pad 43: Net-(D3-Pad43) -> /Lattice MACHXO2/Digit_1/D1A3
- D3 pad 430: Net-(D3-Pad430) -> /Lattice MACHXO2/Digit_4/D4A6
- D3 pad 431: Net-(D3-Pad431) -> Net-(D3-Pad416)
- D3 pad 432: Net-(D3-Pad432) -> Net-(D3-Pad417)
- D3 pad 433: Net-(D3-Pad433) -> /Lattice MACHXO2/Digit_4/D4A1
- D3 pad 436: Net-(D3-Pad436) -> /Lattice MACHXO2/Digit_4/D4A2
- D3 pad 437: Net-(D3-Pad437) -> Net-(D3-Pad434)
- D3 pad 438: Net-(D3-Pad438) -> Net-(D3-Pad435)
- D3 pad 439: Net-(D3-Pad439) -> /Lattice MACHXO2/Digit_4/D4A3
- D3 pad 44: Net-(D3-Pad44) -> Net-(D3-Pad38)
- D3 pad 440: Net-(D3-Pad440) -> Net-(D3-Pad434)
- D3 pad 441: Net-(D3-Pad441) -> Net-(D3-Pad435)
- D3 pad 442: Net-(D3-Pad442) -> /Lattice MACHXO2/Digit_4/D4A4
- D3 pad 443: Net-(D3-Pad443) -> Net-(D3-Pad434)
- D3 pad 444: Net-(D3-Pad444) -> Net-(D3-Pad435)
- D3 pad 445: Net-(D3-Pad445) -> /Lattice MACHXO2/Digit_4/D4A5
- D3 pad 446: Net-(D3-Pad446) -> Net-(D3-Pad434)
- D3 pad 447: Net-(D3-Pad447) -> Net-(D3-Pad435)
- D3 pad 448: Net-(D3-Pad448) -> /Lattice MACHXO2/Digit_4/D4A6
- D3 pad 449: Net-(D3-Pad449) -> Net-(D3-Pad434)
- D3 pad 45: Net-(D3-Pad45) -> Net-(D3-Pad39)
- D3 pad 450: Net-(D3-Pad450) -> Net-(D3-Pad435)
- D3 pad 451: Net-(D3-Pad451) -> /Lattice MACHXO2/Digit_4/D4A1
- D3 pad 454: Net-(D3-Pad454) -> /Lattice MACHXO2/Digit_4/D4A2
- D3 pad 455: Net-(D3-Pad455) -> Net-(D3-Pad452)
- D3 pad 456: Net-(D3-Pad456) -> Net-(D3-Pad453)
- D3 pad 457: Net-(D3-Pad457) -> /Lattice MACHXO2/Digit_4/D4A3
- D3 pad 458: Net-(D3-Pad458) -> Net-(D3-Pad452)
- D3 pad 459: Net-(D3-Pad459) -> Net-(D3-Pad453)
- D3 pad 46: Net-(D3-Pad46) -> /Lattice MACHXO2/Digit_1/D1A4
- D3 pad 460: Net-(D3-Pad460) -> /Lattice MACHXO2/Digit_4/D4A4
- D3 pad 461: Net-(D3-Pad461) -> Net-(D3-Pad452)
- D3 pad 462: Net-(D3-Pad462) -> Net-(D3-Pad453)
- D3 pad 463: Net-(D3-Pad463) -> /Lattice MACHXO2/Digit_4/D4A5
- D3 pad 464: Net-(D3-Pad464) -> Net-(D3-Pad452)
- D3 pad 465: Net-(D3-Pad465) -> Net-(D3-Pad453)
- D3 pad 466: Net-(D3-Pad466) -> /Lattice MACHXO2/Digit_4/D4A6
- D3 pad 467: Net-(D3-Pad467) -> Net-(D3-Pad452)
- D3 pad 468: Net-(D3-Pad468) -> Net-(D3-Pad453)
- D3 pad 469: Net-(D3-Pad469) -> /Lattice MACHXO2/Digit_4/D4A1
- D3 pad 47: Net-(D3-Pad47) -> Net-(D3-Pad38)
- D3 pad 472: Net-(D3-Pad472) -> /Lattice MACHXO2/Digit_4/D4A2
- D3 pad 473: Net-(D3-Pad473) -> Net-(D3-Pad470)
- D3 pad 474: Net-(D3-Pad474) -> Net-(D3-Pad471)
- D3 pad 475: Net-(D3-Pad475) -> /Lattice MACHXO2/Digit_4/D4A3
- D3 pad 476: Net-(D3-Pad476) -> Net-(D3-Pad470)
- D3 pad 477: Net-(D3-Pad477) -> Net-(D3-Pad471)
- D3 pad 478: Net-(D3-Pad478) -> /Lattice MACHXO2/Digit_4/D4A4
- D3 pad 479: Net-(D3-Pad479) -> Net-(D3-Pad470)
- D3 pad 48: Net-(D3-Pad48) -> Net-(D3-Pad39)
- D3 pad 480: Net-(D3-Pad480) -> Net-(D3-Pad471)
- D3 pad 481: Net-(D3-Pad481) -> /Lattice MACHXO2/Digit_4/D4A5
- D3 pad 482: Net-(D3-Pad482) -> Net-(D3-Pad470)
- D3 pad 483: Net-(D3-Pad483) -> Net-(D3-Pad471)
- D3 pad 484: Net-(D3-Pad484) -> /Lattice MACHXO2/Digit_4/D4A6
- D3 pad 485: Net-(D3-Pad485) -> Net-(D3-Pad470)
- D3 pad 486: Net-(D3-Pad486) -> Net-(D3-Pad471)
- D3 pad 487: Net-(D3-Pad487) -> /Lattice MACHXO2/Digit_4/D4A1
- D3 pad 49: Net-(D3-Pad49) -> /Lattice MACHXO2/Digit_1/D1A5
- D3 pad 490: Net-(D3-Pad490) -> /Lattice MACHXO2/Digit_4/D4A2
- D3 pad 491: Net-(D3-Pad491) -> Net-(D3-Pad488)
- D3 pad 492: Net-(D3-Pad492) -> Net-(D3-Pad489)
- D3 pad 493: Net-(D3-Pad493) -> /Lattice MACHXO2/Digit_4/D4A3
- D3 pad 494: Net-(D3-Pad494) -> Net-(D3-Pad488)
- D3 pad 495: Net-(D3-Pad495) -> Net-(D3-Pad489)
- D3 pad 496: Net-(D3-Pad496) -> /Lattice MACHXO2/Digit_4/D4A4
- D3 pad 497: Net-(D3-Pad497) -> Net-(D3-Pad488)
- D3 pad 498: Net-(D3-Pad498) -> Net-(D3-Pad489)
- D3 pad 499: Net-(D3-Pad499) -> /Lattice MACHXO2/Digit_4/D4A5
- D3 pad 5: Net-(D3-Pad5) -> Net-(D3-Pad11)
- D3 pad 50: Net-(D3-Pad50) -> Net-(D3-Pad38)
- D3 pad 500: Net-(D3-Pad500) -> Net-(D3-Pad488)
- D3 pad 501: Net-(D3-Pad501) -> Net-(D3-Pad489)
- D3 pad 502: Net-(D3-Pad502) -> /Lattice MACHXO2/Digit_4/D4A6
- D3 pad 503: Net-(D3-Pad503) -> Net-(D3-Pad488)
- D3 pad 504: Net-(D3-Pad504) -> Net-(D3-Pad489)
- D3 pad 51: Net-(D3-Pad51) -> Net-(D3-Pad39)
- D3 pad 52: Net-(D3-Pad52) -> /Lattice MACHXO2/Digit_1/D1A6
- D3 pad 53: Net-(D3-Pad53) -> Net-(D3-Pad38)
- D3 pad 54: Net-(D3-Pad54) -> Net-(D3-Pad39)
- D3 pad 55: Net-(D3-Pad55) -> /Lattice MACHXO2/Digit_1/D1A1
- D3 pad 58: Net-(D3-Pad58) -> /Lattice MACHXO2/Digit_1/D1A2
- D3 pad 59: Net-(D3-Pad59) -> Net-(D3-Pad56)
- D3 pad 6: Net-(D3-Pad6) -> Net-(D3-Pad12)
- D3 pad 60: Net-(D3-Pad60) -> Net-(D3-Pad57)
- D3 pad 61: Net-(D3-Pad61) -> /Lattice MACHXO2/Digit_1/D1A3
- D3 pad 62: Net-(D3-Pad62) -> Net-(D3-Pad56)
- D3 pad 63: Net-(D3-Pad63) -> Net-(D3-Pad57)
- D3 pad 64: Net-(D3-Pad64) -> /Lattice MACHXO2/Digit_1/D1A4
- D3 pad 65: Net-(D3-Pad65) -> Net-(D3-Pad56)
- D3 pad 66: Net-(D3-Pad66) -> Net-(D3-Pad57)
- D3 pad 67: Net-(D3-Pad67) -> /Lattice MACHXO2/Digit_1/D1A5
- D3 pad 68: Net-(D3-Pad68) -> Net-(D3-Pad56)
- D3 pad 69: Net-(D3-Pad69) -> Net-(D3-Pad57)
- D3 pad 7: Net-(D3-Pad7) -> /Lattice MACHXO2/Digit_1/D1A3
- D3 pad 70: Net-(D3-Pad70) -> /Lattice MACHXO2/Digit_1/D1A6
- D3 pad 71: Net-(D3-Pad71) -> Net-(D3-Pad56)
- D3 pad 72: Net-(D3-Pad72) -> Net-(D3-Pad57)
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
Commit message: Edit PCB.
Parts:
- added Q30: DMN2041LSD-13, SO-8, F.Cu at (208.3, 41.9)
- added Q31: DMN2041LSD-13, SO-8, F.Cu at (214.6, 41.9)
- added Q32: DMN2041LSD-13, SO-8, F.Cu at (221.0, 41.9)
- added Q33: DMN2041LSD-13, SO-8, F.Cu at (119.4, 41.9)
- added Q34: DMN2041LSD-13, SO-8, F.Cu at (127.0, 41.9)
- added Q35: DMN2041LSD-13, SO-8, F.Cu at (134.6, 41.9)
- added Q36: DMN2041LSD-13, SO-8, F.Cu at (174.0, 41.9)
- added Q37: DMN2041LSD-13, SO-8, F.Cu at (181.6, 41.9)
- added Q38: DMN2041LSD-13, SO-8, F.Cu at (166.4, 41.9)
- added Q39: DMN2041LSD-13, SO-8, F.Cu at (76.2, 41.9)
- added Q40: DMN2041LSD-13, SO-8, F.Cu at (83.8, 41.9)
- added Q41: DMN2041LSD-13, SO-8, F.Cu at (91.4, 41.9)
- added R100: 10K, Resistors_SMD:R_0603_HandSoldering, F.Cu at (87.6, 157.5)
- added R101: 150, Resistors_SMD:R_0603_HandSoldering, F.Cu at (71.1, 34.3)
- added R102: 150, Resistors_SMD:R_0603_HandSoldering, F.Cu at (76.2, 34.3)
- added R103: 10K, Resistors_SMD:R_0603_HandSoldering, F.Cu at (147.5, 155.1)
- added R104: 10K, Resistors_SMD:R_0603_HandSoldering, F.Cu at (90.2, 144.8)
- added R105: 150, Resistors_SMD:R_0603_HandSoldering, F.Cu at (82.5, 34.3)
- added R106: 150, Resistors_SMD:R_0603_HandSoldering, F.Cu at (87.6, 34.3)
- added R107: 10K, Resistors_SMD:R_0603_HandSoldering, F.Cu at (129.5, 164.2)
- added R108: 10K, Resistors_SMD:R_0603_HandSoldering, F.Cu at (142.2, 129.5)
- added R109: 150, Resistors_SMD:R_0603_HandSoldering, F.Cu at (95.2, 34.3)
- added R110: 150, Resistors_SMD:R_0603_HandSoldering, F.Cu at (100.3, 34.3)
- added R63: 10K, Resistors_SMD:R_0603_HandSoldering, F.Cu at (203.3, 179.3)
- added R64: 10K, Resistors_SMD:R_0603_HandSoldering, F.Cu at (185.3, 192.9)
- added R65: 150, Resistors_SMD:R_0603_HandSoldering, F.Cu at (180.7, 200.4)
- added R66: 150, Resistors_SMD:R_0603_HandSoldering, F.Cu at (204.5, 33.0)
- added R67: 10K, Resistors_SMD:R_0603_HandSoldering, F.Cu at (185.2, 186.9)
- added R68: 10K, Resistors_SMD:R_0603_HandSoldering, F.Cu at (189.8, 186.9)
- added R69: 150, Resistors_SMD:R_0603_HandSoldering, F.Cu at (171.6, 200.4)
- added R70: 150, Resistors_SMD:R_0603_HandSoldering, F.Cu at (180.7, 194.4)
- added R71: 10K, Resistors_SMD:R_0603_HandSoldering, F.Cu at (198.8, 179.3)
- added R72: 10K, Resistors_SMD:R_0603_HandSoldering, F.Cu at (176.2, 194.4)
- added R73: 150, Resistors_SMD:R_0603_HandSoldering, F.Cu at (171.6, 194.4)
- added R74: 150, Resistors_SMD:R_0603_HandSoldering, F.Cu at (222.2, 33.0)
- added R75: 10K, Resistors_SMD:R_0603_HandSoldering, F.Cu at (143.1, 197.3)
- added R76: 10K, Resistors_SMD:R_0603_HandSoldering, F.Cu at (156.6, 185.3)
- added R77: 150, Resistors_SMD:R_0603_HandSoldering, F.Cu at (147.6, 191.3)
- added R78: 150, Resistors_SMD:R_0603_HandSoldering, F.Cu at (118.1, 33.0)
- added R79: 10K, Resistors_SMD:R_0603_HandSoldering, F.Cu at (134.0, 198.9)
- added R80: 10K, Resistors_SMD:R_0603_HandSoldering, F.Cu at (152.1, 185.3)
- added R81: 150, Resistors_SMD:R_0603_HandSoldering, F.Cu at (156.6, 179.3)
- added R82: 150, Resistors_SMD:R_0603_HandSoldering, F.Cu at (125.7, 33.0)
- added R83: 10K, Resistors_SMD:R_0603_HandSoldering, F.Cu at (133.9, 186.9)
- added R84: 10K, Resistors_SMD:R_0603_HandSoldering, F.Cu at (152.1, 191.3)
- added R85: 150, Resistors_SMD:R_0603_HandSoldering, F.Cu at (139.7, 33.0)
- added R86: 150, Resistors_SMD:R_0603_HandSoldering, F.Cu at (133.3, 33.0)
- added R87: 10K, Resistors_SMD:R_0603_HandSoldering, F.Cu at (203.5, 167.1)
- added R88: 10K, Resistors_SMD:R_0603_HandSoldering, F.Cu at (208.0, 161.1)
- added R89: 150, Resistors_SMD:R_0603_HandSoldering, F.Cu at (172.7, 33.0)
- added R90: 150, Resistors_SMD:R_0603_HandSoldering, F.Cu at (212.4, 155.1)
- added R91: 10K, Resistors_SMD:R_0603_HandSoldering, F.Cu at (203.4, 161.1)
- added R92: 10K, Resistors_SMD:R_0603_HandSoldering, F.Cu at (212.4, 149.1)
- added R93: 150, Resistors_SMD:R_0603_HandSoldering, F.Cu at (180.3, 33.0)
- added R94: 150, Resistors_SMD:R_0603_HandSoldering, F.Cu at (207.9, 155.1)
- added R95: 10K, Resistors_SMD:R_0603_HandSoldering, F.Cu at (189.8, 156.7)
- added R96: 10K, Resistors_SMD:R_0603_HandSoldering, F.Cu at (176.2, 170.2)
- added R97: 150, Resistors_SMD:R_0603_HandSoldering, F.Cu at (158.8, 33.0)
- added R98: 150, Resistors_SMD:R_0603_HandSoldering, F.Cu at (163.8, 33.0)
- added R99: 10K, Resistors_SMD:R_0603_HandSoldering, F.Cu at (143.0, 161.1)
- R3: value 1K -> 150
- moved R3 180.4 mm to (251.5, 148.6)
- moved R17 55.3 mm to (129.5, 200.4)
- moved R15 55.3 mm to (124.9, 200.4)
- moved R13 50.4 mm to (120.4, 200.4)
- moved R9 47.8 mm to (120.4, 194.4)
- moved R31 45.2 mm to (171.6, 170.2)
- moved Q25 44.1 mm to (45.7, 66.0)
- moved R46 42.9 mm to (189.8, 197.3)
- moved R36 40.0 mm to (176.2, 200.4)
- moved R18 38.9 mm to (134.0, 192.9)
- moved R35 38.5 mm to (207.9, 179.3)
- moved R12 38.0 mm to (129.5, 194.4)
- moved R22 37.7 mm to (180.7, 170.2)
- moved R39 37.5 mm to (198.9, 197.3)
- moved Q26 37.4 mm to (47.0, 91.4)
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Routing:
- net /Lattice MACHXO2/Digit_1/D1A5: track 0.00 -> 29.4 mm
- net /Lattice MACHXO2/Digit_1/D1A6: track 0.00 -> 13.8 mm
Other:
- net class Default: clearance 0.254 -> 0.2032; trace_width 0.254 -> 0.2032
- net class LED Routes added: clearance 0.2032, trace_width 0.2032, via_dia 0.889, via_drill 0.635
- rule trace_clearance: 0.254 -> 0.2032
- rule trace_min: 0.254 -> 0.1524
